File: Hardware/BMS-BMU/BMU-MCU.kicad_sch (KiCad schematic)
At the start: 7 parts, among them IC1 STM32C092RCT6, J2 Conn_ARM_JTAG_SWD_10

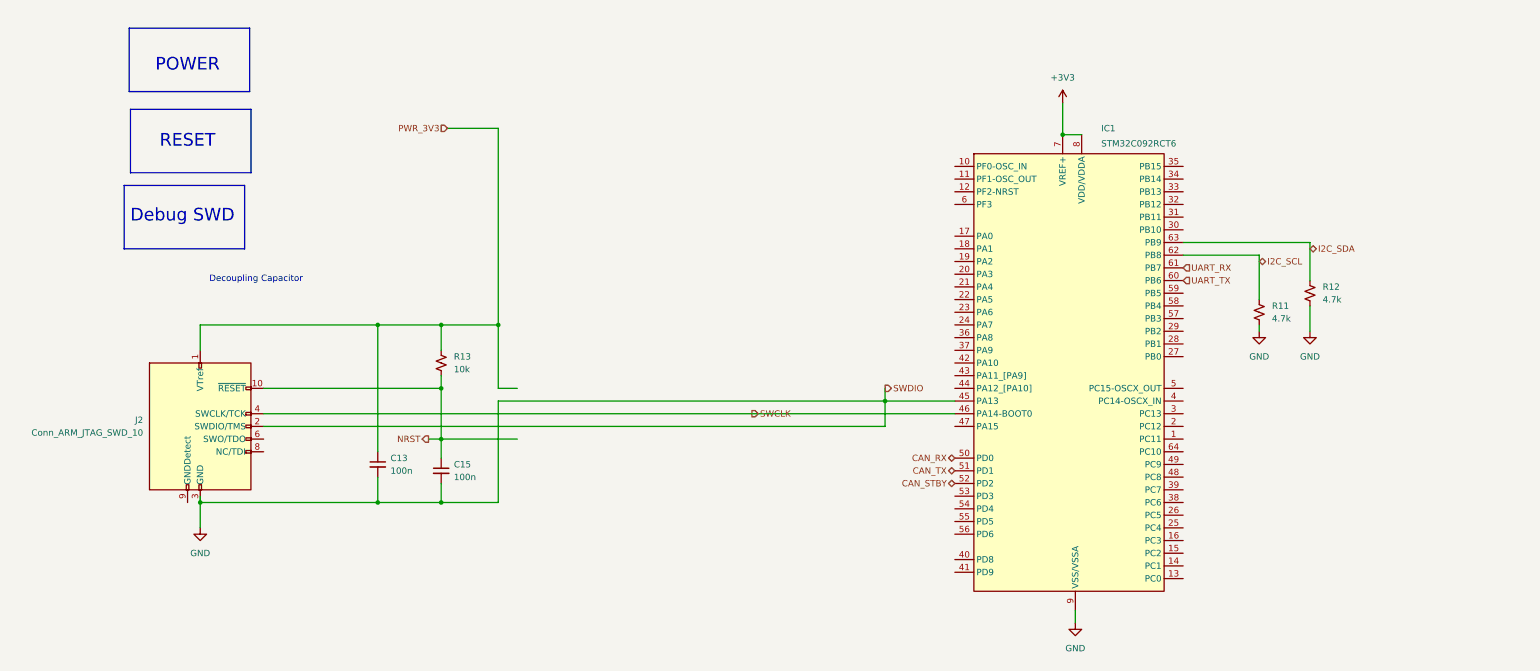
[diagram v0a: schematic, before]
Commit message: update CAN and SHUNT IF
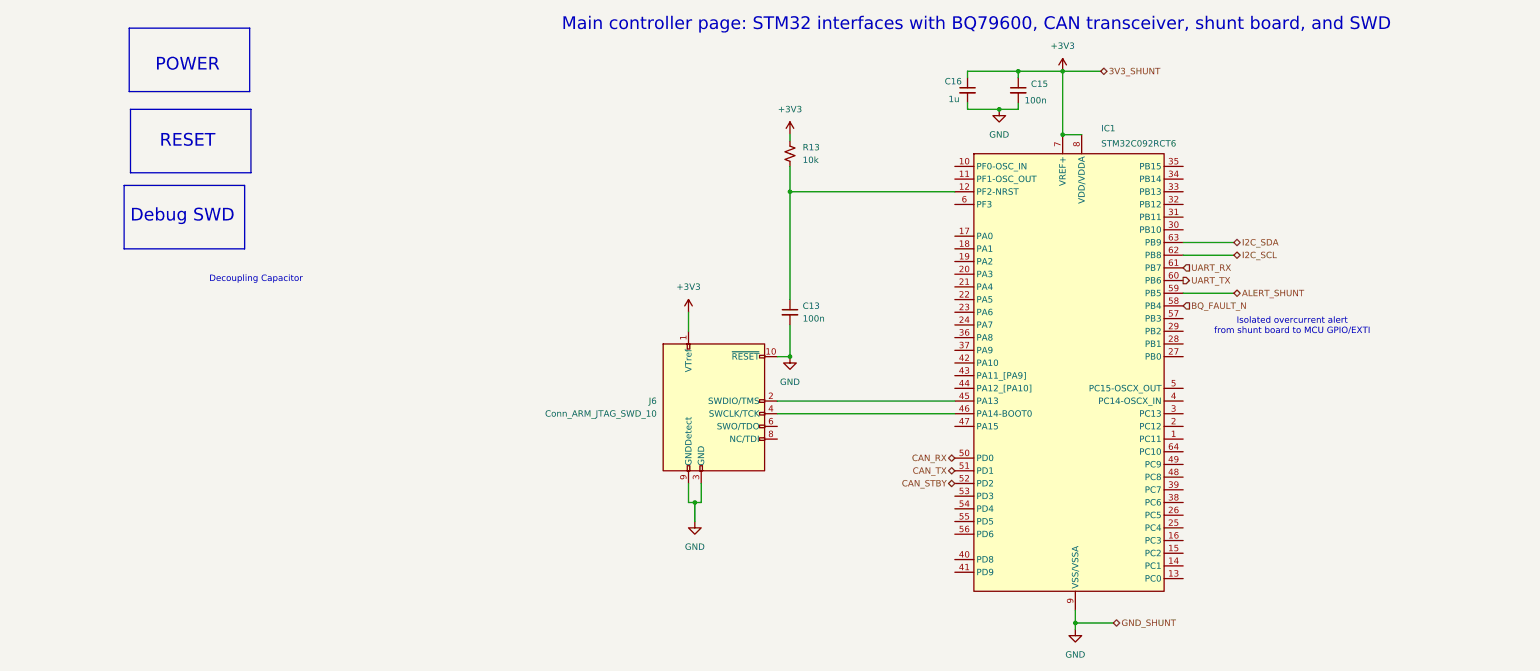
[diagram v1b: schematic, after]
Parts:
- removed R11, R12: 4.7k, symbol Device:R_Small_US
- added C16: 1u, symbol Device:C_Small
- renumbered J2 to J6
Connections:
- net +3V3: now also C15.1, J6.1 (VTref), R13.1, C16.1
- net GND: now also J6.10 (~{RESET}), J6.9 (GNDDetect), C16.2; no longer IC1.45 (PA13), J6.2 (SWDIO/TMS)
- net at IC1.12 (PF2-NRST): now also C13.1, R13.2
- net BQ_FAULT_N: now reaches IC1.58 (PB4)
- net ALERT_SHUNT: now reaches IC1.59 (PB5)
- removed net NRST: C15.1, J6.10 (~{RESET}), R13.2
- removed net PWR_3V3: C13.1, J6.1 (VTref), R13.1
- net SWCLK: no longer names the net of IC1.46 (PA14-BOOT0), J6.4 (SWCLK/TCK)
- new net: IC1.45 (PA13), J6.2 (SWDIO/TMS)
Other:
- note added: "Isolated overcurrent alert from shunt board to MCU GPIO/EXTI"
- note added: "Main controller page: STM32 interfaces with BQ79600, CAN transceiver, shunt board, and SWD"
- moved on the sheet: C13, J6, R13
